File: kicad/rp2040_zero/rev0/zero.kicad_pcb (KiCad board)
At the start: 2 copper layers, 41.8 x 30.2 mm, 22 parts, among them J1 jtag, J2 Conn_01x03_Socket, J5 Debug port, U1 RP2040-Zero, U3 3V->VTREF, U4 VTREF->3V, U5 VTREF<->3V, U6 RT9013-33GB

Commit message: kicad: update to correct voltage translator footprint
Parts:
- removed kibuzzard-6719D5F3: G***, kibuzzard-6719D5F3
- removed kibuzzard-6719D670: G***, kibuzzard-6719D670
- added kibuzzard-6719D73B: G***, kibuzzard-6719D73B, F.Cu at (114.5, 67.7)
- added kibuzzard-67310D89: G***, kibuzzard-67310D89, F.Cu at (117.4, 71.7)
- added kibuzzard-67310DA4: G***, kibuzzard-67310DA4, F.Cu at (117.2, 73.7)
- U3, U4, U5: footprint Package_SO:VSSOP-8_2.3x2mm_P0.5mm -> Package_SO:TSSOP-8_3x3mm_P0.65mm
- moved C1 5.21 mm to (120.3, 71.7), turned to 180 degrees
- moved U4 0.58 mm to (121.2, 83.6)
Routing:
- net VTREF: track 30.2 -> 33.0 mm
- net OUT_SWDCLK: track 25.8 -> 28.3 mm
- net +3.3V: track 55.6 -> 57.7 mm
- net SWIO_DIR_3V: track 12.0 -> 10.5 mm
- net GND: track 111.4 -> 112.4 mm, vias 8 -> 9
- net OUT_UART_RX: track 19.1 -> 18.1 mm
- net OUT_SWDIO: track 25.1 -> 24.3 mm
- net OUT_SWDIO_3V: track 4.31 -> 3.49 mm
- net OUT_SWDCLK_3V: track 11.0 -> 10.3 mm

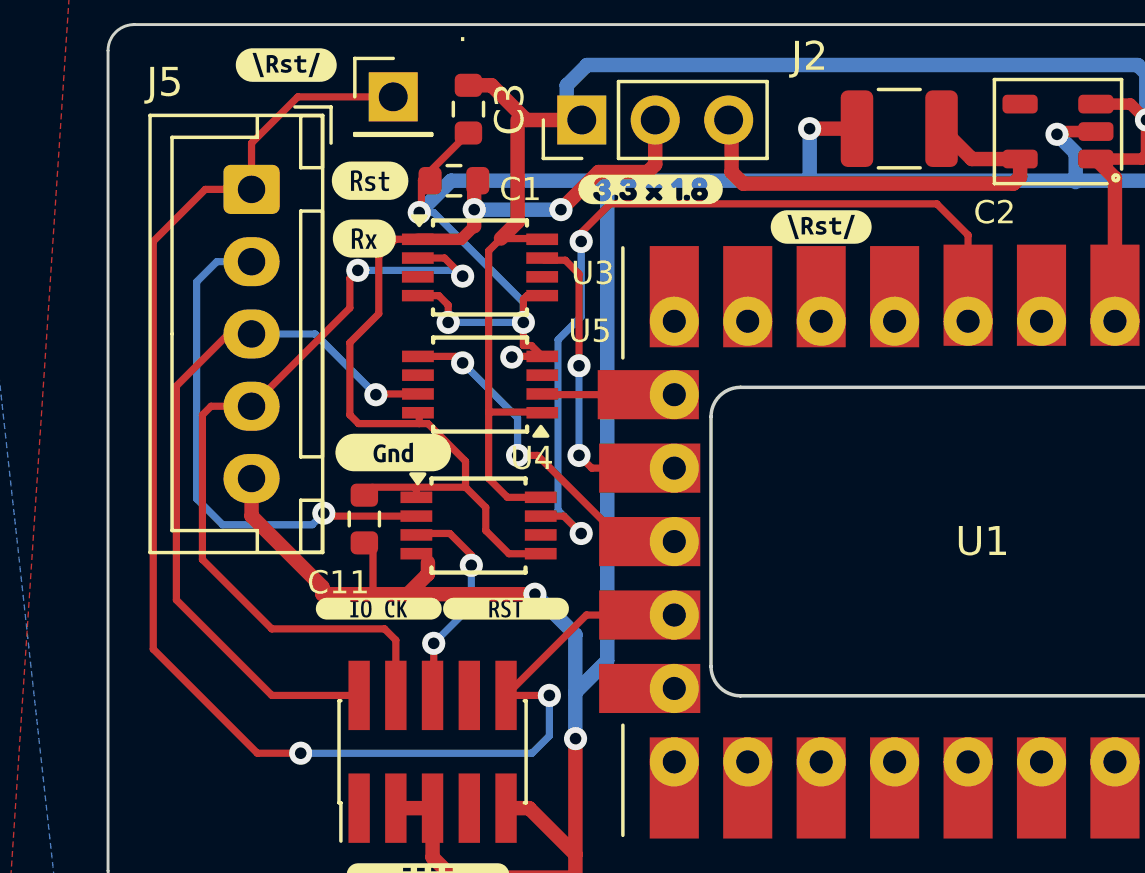
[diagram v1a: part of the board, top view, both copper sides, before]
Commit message: kicad : map the uart RX to GPIO9 on the carrier
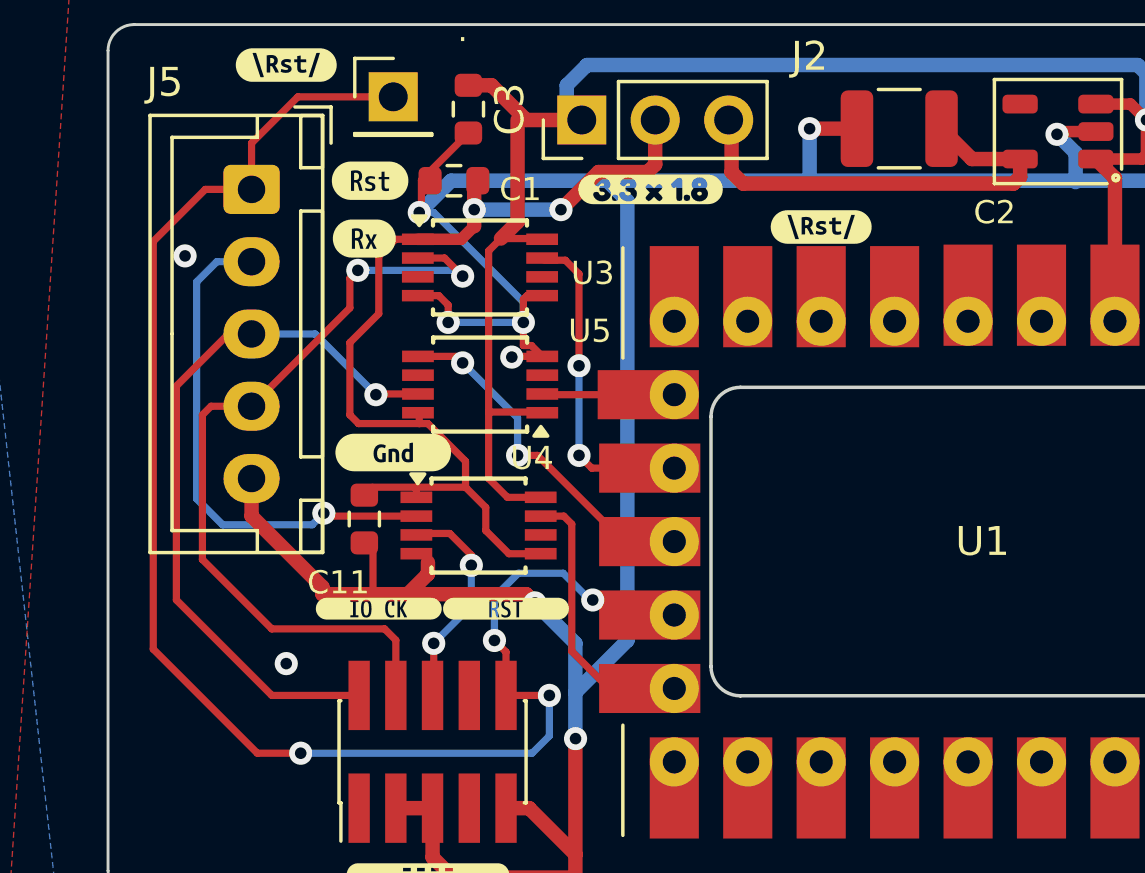
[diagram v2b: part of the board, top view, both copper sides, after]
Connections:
- U1 pad 23: unconnected-(U1-GP9-Pad23) -> OUT_UART_RX_3V
- U1 pad 5: OUT_UART_RX_3V -> unconnected-(U1-GP28-Pad5)
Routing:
- net OUT_UART_RX_3V: track 29.0 -> 7.41 mm, vias 2 -> 0
- net INOUT_NRESET: track 49.9 -> 52.8 mm, vias 2 -> 4
- net GND: track 112.4 -> 113.0 mm, vias 9 -> 11
